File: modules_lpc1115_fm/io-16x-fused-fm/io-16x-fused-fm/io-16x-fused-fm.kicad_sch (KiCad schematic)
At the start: 143 parts, among them IC5 LPC1115, IC6 ATAES132A-SHEQ-T, J1 62000611622, J2 1771017, J3 1770953, Q3 ASF, U3 EEPROM, X1 MICROMATCH-10SMD

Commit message: convert io-16x-fused-fm WIP
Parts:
- C1, C2, C25, C26, C27, C28, C29, C30, C31, C32, C33, C34, C35, C36: footprint io-16x-fused-fm:C0805 -> Capacitor_SMD:C_0805_2012Metric; symbol io-16x-fused-fm-eagle-import:C-EUC0805 -> Device:C
- D1, D13, D14, D15, D16, D17, D18, D19, D2, D20, D3, D4, D5, D6, D7, D8: footprint io-16x-fused-fm:SOD-123 -> Diode_SMD:D_SOD-123; symbol io-16x-fused-fm-eagle-import:DIODE-ZENERSOD-123 -> Device:D_Zener
- D10, D11, D12, D21, D22, D23, D24, D9: footprint io-16x-fused-fm:SOT23 -> Package_TO_SOT_SMD:SOT-23; symbol io-16x-fused-fm-eagle-import:BAT54C -> Diode:BAT54C
- F1, F10, F11, F12, F13, F14, F15, F16, F2, F3, F4, F5, F6, F7, F8, F9: footprint io-16x-fused-fm:0805L -> Fuse:Fuse_0805_2012Metric; symbol io-16x-fused-fm-eagle-import:?0805L -> Device:Polyfuse
- FB1, FB17, FB18, FB19, FB2, FB20, FB21, FB22, FB23, FB24, FB3, FB4, FB5, FB6, FB7, FB8: footprint io-16x-fused-fm:FERR_0805MP -> Inductor_SMD:L_0805_2012Metric; symbol io-16x-fused-fm-eagle-import:FERRITE2_0805MP -> Device:FerriteBead
- IC6: footprint io-16x-fused-fm:SOIC127P600X175-8N -> Package_SO:SOIC-8_3.9x4.9mm_P1.27mm; symbol io-16x-fused-fm-eagle-import:ATAES132A-SHEQ-T -> Memory_EEPROM:25LCxxx
- J2: symbol io-16x-fused-fm-eagle-import:1771017 -> Connector_Generic:Conn_01x08
- J3: symbol io-16x-fused-fm-eagle-import:1770953 -> Connector_Generic:Conn_01x02
- JP1: value PINHD-1X06_2.54-S -> Conn_01x06_Pin; symbol io-16x-fused-fm-eagle-import:PINHD-1X06_2.54-S -> Connector:Conn_01x06_Pin
- JP17: value J -> Conn_02x05_Odd_Even; symbol io-16x-fused-fm-eagle-import:PINHD-2X05_2.00 -> Connector_Generic:Conn_02x05_Odd_Even
- JP18, JP21, JP24: symbol io-16x-fused-fm-eagle-import:PINHD-1X2 -> Connector:Conn_01x02_Pin
- JP2: symbol io-16x-fused-fm-eagle-import:PINHD-1X5 -> Connector:Conn_01x05_Pin
- JP22: symbol io-16x-fused-fm-eagle-import:62000411622 -> Connector:Conn_01x04_Pin
- JP23: value PINHD-1X4 -> Conn_01x04_Pin; symbol io-16x-fused-fm-eagle-import:PINHD-1X4 -> Connector:Conn_01x04_Pin
- LED5, LED6: footprint io-16x-fused-fm:CHIPLED_0805 -> LED_SMD:LED_0805_2012Metric; symbol io-16x-fused-fm-eagle-import:LEDCHIPLED_0805 -> Device:LED
- PRGBTN2: footprint io-16x-fused-fm:1X01 -> Connector_PinSocket_2.54mm:PinSocket_1x01_P2.54mm_Horizontal; symbol io-16x-fused-fm-eagle-import:PINHD-1X1 -> Connector:Conn_01x01_Pin
- R1, R10, R11, R12, R13, R14, R15, R16, R2, R3, R4, R5, R55, R56, R57, R58, R59, R6, R60, R61, R62, R63, R64, R65, R66, R67, R68, R69, R7, R70, R71, R72, R73, R74, R75, R76, R77, R78, R79, R8, R80, R81, R9: footprint io-16x-fused-fm:R0805 -> Resistor_SMD:R_0805_2012Metric; symbol io-16x-fused-fm-eagle-import:R-EU_R0805 -> Device:R
- TP1, TP2, TP3, TP4, TP5, TP6: footprint io-16x-fused-fm:TP08R -> TestPoint:TestPoint_Pad_D1.0mm; symbol io-16x-fused-fm-eagle-import:TPSQTP08R -> Connector:TestPoint
- TVS1, TVS2, TVS5, TVS6, TVS9: footprint io-16x-fused-fm:SOT-23-6L -> Package_TO_SOT_SMD:SOT-23-6; symbol io-16x-fused-fm-eagle-import:USBLC6-4SC6 -> Power_Protection:USBLC6-4SC6
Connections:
- net +3V3: now also J3.2 (Pin_2), JP22.2 (Pin_2), LED6.2 (A); no longer IC6.3 (NC_1), IC6.7 (NC_2), J3.3 (2.1), J3.4 (2.2), JP22.3
- net GND: now also D1.2 (A), D13.2 (A), D14.2 (A), D15.2 (A), D16.2 (A), D17.2 (A), D18.2 (A), D19.2 (A), D2.2 (A), D20.2 (A), D3.2 (A), D4.2 (A), D5.2 (A), D6.2 (A), D7.2 (A), D8.2 (A), JP22.1 (Pin_1); no longer D1.A, D13.A, D14.A, D15.A, D16.A, D17.A, D18.A, D19.A, D2.A, D20.A, D3.A, D4.A, D5.A, D6.A, D7.A, D8.A, J3.2 (1.2), JP22.4
- net IN1: no longer J2.2 (1.2)
- net IN2: now also J2.2 (Pin_2); no longer J2.3 (2.1), J2.4 (2.2)
- net IN3: now also J2.3 (Pin_3); no longer J2.5 (3.1), J2.6 (3.2)
- net IN4: now also J2.4 (Pin_4); no longer J2.7 (4.1), J2.8 (4.2)
- net IN5: now also J2.5 (Pin_5); no longer J2.10 (5.2), J2.9 (5.1)
- net IN6: now also J2.6 (Pin_6); no longer J2.11 (6.1), J2.12 (6.2)
- net IN7: now also J2.7 (Pin_7); no longer J2.13 (7.1), J2.14 (7.2)
- net IN8: now also J2.8 (Pin_8); no longer J2.15 (8.1), J2.16 (8.2)
- net IO1R: now also D19.1 (K); no longer D19.C
- net IO2R: now also D20.1 (K); no longer D20.C
- net IO3R: now also D17.1 (K); no longer D17.C
- net IO4R: now also D18.1 (K); no longer D18.C
- net IO5R: now also D13.1 (K); no longer D13.C
- net IO6R: now also D14.1 (K); no longer D14.C
- net IO7R: now also D16.1 (K); no longer D16.C
- net IO8R: now also D15.1 (K); no longer D15.C
- net N$10: now also F5.1; no longer F5.2
- net N$11: now also F10.1; no longer F10.2
- net N$12: now also F6.1; no longer F6.2
- net N$13: now also F15.1; no longer F15.2
- net N$14: now also F7.1; no longer F7.2
- net N$15: now also F11.1; no longer F11.2
- net N$16: now also F16.1; no longer F16.2
- net N$17: now also F8.1; no longer F8.2
- net N$2: now also F13.1; no longer F13.2
- net N$3: now also F14.1; no longer F14.2
- net N$4: now also F12.1; no longer F12.2
- net N$5: now also F9.1; no longer F9.2
- net PROG: now also LED5.1 (K); no longer LED5.C
- net SCL: now also JP22.4 (Pin_4); no longer JP22.1
- net SDA: now also JP22.3 (Pin_3); no longer JP22.2
- net at FB7.2: now also F7.2; no longer F7.1
- net at FB5.2: now also F5.2; no longer F5.1
- net at IC5.32 (TDI/PIO0_11/AD0/CT32B0_MAT3): now also TP2.1; no longer TP2.TP
- net at D10.2, R1.2, R12.1: now also D1.1 (K); no longer D1.C
- net at FB18.1: now also F10.2; no longer F10.1
- net at D10.1, R2.2, R9.1: now also D2.1 (K); no longer D2.C
- net at D11.2, R14.1, R7.2: now also D6.1 (K); no longer D6.C
- net at D9.1, R10.1, R3.2: now also D3.1 (K); no longer D3.C
- net at D9.2, R11.1, R4.2: now also D4.1 (K); no longer D4.C
- net at IC5.45 (PIO1_5/RTS/CT32B0_CAP0): now also TP6.1; no longer TP6.TP
- net at R1.1: now also F1.1, TVS1.4 (I/O3); no longer F1.2
- net at R57.1: now also LED5.2 (A); no longer LED5.A
- net at FB17.1: now also F9.2; no longer F9.1
- net at IC5.34 (TDO/PIO1_1/AD2/CT32B1_MAT0): now also TP4.1; no longer TP4.TP
- net at FB8.2: now also F8.2; no longer F8.1
- net at D11.1, R15.1, R8.2: now also D5.1 (K); no longer D5.C
- net at D12.2, R13.1, R6.2: now also D7.1 (K); no longer D7.C
- net at D12.1, R16.1, R5.2: now also D8.1 (K); no longer D8.C
- net at FB20.1: now also F12.2; no longer F12.1
- net at IC5.33 (TMS/PIO1_0/AD1/CT32B1_CAP0): now also TP3.1; no longer TP3.TP
- net at IC5.31 (PIO2_11/SCK0/CT32B0_CAP1): now also TP1.1; no longer TP1.TP
- net at FB19.1: now also F11.2; no longer F11.1
- net at R3.1, TVS1.6 (I/O4): now also F3.1; no longer F3.2
- net at FB6.2: now also F6.2; no longer F6.1
- net at F4.1: now also R4.1, TVS1.1 (I/O1); no longer FB4.1 (P$1)
- net at FB23.1: now also F14.2; no longer F14.1
- net at FB21.1: now also F16.2; no longer F16.1
- net at R2.1, TVS1.3 (I/O2): now also F2.1; no longer F2.2
- net at FB3.1: now also F3.2; no longer F3.1
- net at FB1.1: now also F1.2; no longer F1.1
- net at R81.2: now also LED6.1 (K); no longer LED6.C
- net at IC5.35 (TRST/PIO1_2/AD3/CT32B1_MAT1): now also TP5.1; no longer TP5.TP
- net at FB2.1: now also F2.2; no longer F2.1
- net at FB24.1: now also F13.2; no longer F13.1
- net at FB22.1: now also F15.2; no longer F15.1
- new net: F4.2, FB4.1
- no-connect marks 0 -> 7
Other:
- moved on the sheet: JP18, JP21, JP22, JP24

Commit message: bump io-16x-fused-fm - conversion mostly done
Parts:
- IC5: value LPC1115 -> LPC1115FBD48-303; footprint io-16x-fused-fm:LQFP48 -> Package_QFP:LQFP-48_7x7mm_P0.5mm; symbol io-16x-fused-fm-eagle-import:LPC1113/4/5_QFP48_XLSERIES -> MCU_NXP_LPC:LPC1115FBD48-303
- J1: value 62000611622 -> Conn_01x06; footprint io-16x-fused-fm:62000611622 -> Connector_JST:JST_PH_B6B-PH-K_1x06_P2.00mm_Vertical; symbol io-16x-fused-fm-eagle-import:62000611622 -> Connector_Generic:Conn_01x06
- J2: footprint io-16x-fused-fm:1771017 -> TerminalBlock_Phoenix:TerminalBlock_Phoenix_PTSM-0,5-8-2.5-V-THR_1x08_P2.50mm_Vertical
- J3: footprint io-16x-fused-fm:1770953 -> TerminalBlock_Phoenix:TerminalBlock_Phoenix_PTSM-0,5-2-2.5-V-THR_1x02_P2.50mm_Vertical
- JP1: footprint io-16x-fused-fm:1X06-S -> Connector_PinHeader_2.54mm:PinHeader_1x06_P2.54mm_Vertical
- JP17: footprint io-16x-fused-fm:2X05M -> Connector_PinHeader_2.00mm:PinHeader_2x05_P2.00mm_Vertical
- JP18, JP21, JP24: footprint io-16x-fused-fm:1X02 -> Connector_PinHeader_2.54mm:PinHeader_1x02_P2.54mm_Vertical
- JP2: footprint io-16x-fused-fm:1X05 -> Connector_PinHeader_2.54mm:PinHeader_1x05_P2.54mm_Vertical
- JP22: value 62000411622 -> Conn_01x04; footprint io-16x-fused-fm:62000411622 -> Connector_JST:JST_PH_B4B-PH-K_1x04_P2.00mm_Vertical; symbol Connector:Conn_01x04_Pin -> Connector_Generic:Conn_01x04
- JP23: footprint io-16x-fused-fm:1X04 -> Connector_PinHeader_2.54mm:PinHeader_1x04_P2.54mm_Vertical
- PRGBTN2: footprint Connector_PinSocket_2.54mm:PinSocket_1x01_P2.54mm_Horizontal -> Connector_PinHeader_2.54mm:PinHeader_1x01_P2.54mm_Vertical; now not fitted; now left out of the parts list
- Q3: value ASF -> 12 MHz; footprint io-16x-fused-fm:ASF -> Oscillator:Oscillator_SMD_SeikoEpson_SG210-4Pin_2.5x2.0mm; symbol io-16x-fused-fm-eagle-import:ASF -> Oscillator:SG-210STF
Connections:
- net +3V3: now also IC6.3 (~{WP}), IC6.7 (~{HOLD}), JP22.3 (Pin_3); no longer JP22.2 (Pin_2)
- net GND: now also JP18.1 (Pin_1), JP22.4 (Pin_4); no longer JP18.2 (Pin_2), JP22.1 (Pin_1)
- net N$10: now also F5.2; no longer F5.1
- net N$11: now also F10.2; no longer F10.1
- net N$12: now also F6.2; no longer F6.1
- net N$13: now also F15.2; no longer F15.1
- net N$14: now also F7.2; no longer F7.1
- net N$15: now also F11.2; no longer F11.1
- net N$16: now also F16.2; no longer F16.1
- net N$17: now also F8.2; no longer F8.1
- net N$2: now also F13.2; no longer F13.1
- net N$3: now also F14.2; no longer F14.1
- net N$4: now also F12.2; no longer F12.1
- net N$5: now also F9.2; no longer F9.1
- net PROG: now also JP18.2 (Pin_2); no longer JP18.1 (Pin_1)
- net SCL: now also JP22.1 (Pin_1); no longer JP22.4 (Pin_4)
- net SDA: now also JP22.2 (Pin_2); no longer JP22.3 (Pin_3)
- net at FB7.2: now also F7.1; no longer F7.2
- net at FB5.2: now also F5.1; no longer F5.2
- net at FB18.1: now also F10.1; no longer F10.2
- net at R1.1, TVS1.4 (I/O3): now also F1.2; no longer F1.1
- net at FB17.1: now also F9.1; no longer F9.2
- net at FB8.2: now also F8.1; no longer F8.2
- net at FB20.1: now also F12.1; no longer F12.2
- net at FB19.1: now also F11.1; no longer F11.2
- net at R3.1, TVS1.6 (I/O4): now also F3.2; no longer F3.1
- net at FB6.2: now also F6.1; no longer F6.2
- net at R4.1, TVS1.1 (I/O1): now also F4.2; no longer F4.1
- net at FB4.1: now also F4.1; no longer F4.2
- net at FB23.1: now also F14.1; no longer F14.2
- net at FB21.1: now also F16.1; no longer F16.2
- net at R2.1, TVS1.3 (I/O2): now also F2.2; no longer F2.1
- net at FB3.1: now also F3.1; no longer F3.2
- net at FB1.1: now also F1.1; no longer F1.2
- net at FB2.1: now also F2.1; no longer F2.2
- net at FB24.1: now also F13.1; no longer F13.2
- net at FB22.1: now also F15.1; no longer F15.2
- no-connect marks 7 -> 5
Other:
- moved on the sheet: C25, C27, C28, C29, C30, C31, C34, F1, F10, F11, F12, F13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

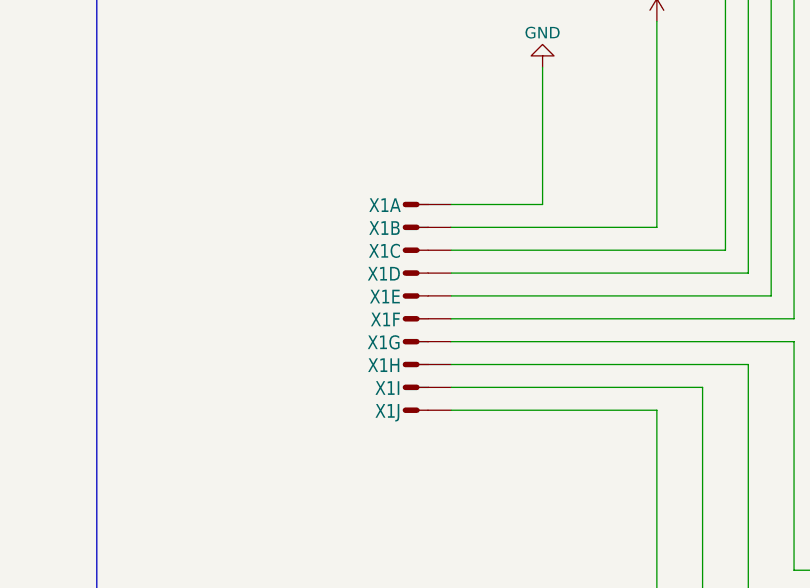
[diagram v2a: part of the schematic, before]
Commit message: io-16x-fused-fm: use micro-match from selfbus library
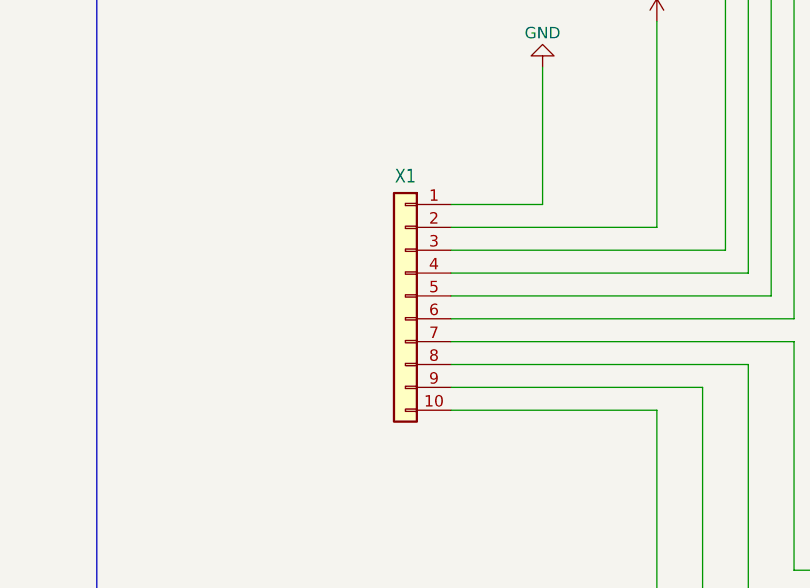
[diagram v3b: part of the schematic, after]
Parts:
- removed unit 10 of X1
- removed unit 3 of X1
- removed unit 5 of X1
- removed unit 7 of X1
- removed unit 4 of X1
- removed unit 8 of X1
- removed unit 6 of X1
- removed unit 2 of X1
- removed unit 9 of X1
- JP1: footprint Connector_PinHeader_2.54mm:PinHeader_1x06_P2.54mm_Vertical -> selfbus:PinHeader_1x06_P2.54mm_Vertical_no_silkscreen
- JP23: footprint Connector_PinHeader_2.54mm:PinHeader_1x04_P2.54mm_Vertical -> selfbus:PinHeader_1x04_P2.54mm_Vertical_no_silkscreen
- U3: footprint io-16x-fused-fm:SOT23-5 -> Package_TO_SOT_SMD:SOT-23-5
- X1: footprint io-16x-fused-fm:MICROMATCH-10SMD -> selfbus:TE_Connectivity_MICRO-MATCH_SMD_FTE_1-188275-0_2x05_P1.27mm_Vertical; symbol io-16x-fused-fm-eagle-import:MICROMATCH-10SMD -> Connector_Generic:Conn_01x10
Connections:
- net +3V3: now also X1.2 (Pin_2)
- net N$22: now also X1.4 (Pin_4)
- net at FB5.1: now also X1.7 (Pin_7)
- net at FB7.1: now also X1.9 (Pin_9)
- net at FB8.1: now also X1.10 (Pin_10)
- net at FB1.2: now also X1.3 (Pin_3)
- net at FB3.2: now also X1.5 (Pin_5)
- net at FB6.1: now also X1.8 (Pin_8)
- net at FB4.2: now also X1.6 (Pin_6)

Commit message: finally standardize selected parts on all boards
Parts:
- C1, C2: value 100nF -> 100n; now left out of the parts list
- C25, C28: value 1uF -> 1u
- C26, C31: value 10nF -> 10n
- C27, C32, C33, C34, C35, C36: value 100nF -> 100n
- C29: value 220pF -> 220p
- C30: value 100pF -> 100p
- D1, D10, D11, D12, D2, D3, D4, D5, D6, D7, D8, D9, FB1, FB2, FB3, FB4, FB5, FB6, FB7, FB8, R1, R10, R11, R12, R13, R14, R15, R16, R2, R3, R4, R5, R6, R7, R8, R9, TVS1, TVS2: now left out of the parts list
- F1, F2, F3, F4, F5, F6, F7, F8: value ?0805L -> BSMD0805-005-33V; now left out of the parts list
- F10, F11, F12, F13, F14, F15, F16, F9: value ?0805L -> BSMD0805-005-33V
- JP1, JP23: now not fitted; now left out of the parts list
- Q3: value 12 MHz -> 12MHz
- R70, R71: value 3,3k -> 3k3
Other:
- note added: "BOTTOM IOs - standardmäßig NICHT auf BOM enthalten"
- note removed: "BOTTOM IOs"

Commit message: final for manufacturing
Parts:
- R10, R11, R12, R13, R14, R15, R16, R73, R74, R75, R76, R77, R78, R79, R80, R9: value 100R -> 100
- U3: value EEPROM -> MCP24AA32 EEPROM; symbol io-16x-fused-fm-eagle-import:EEPROM_I2C_MCP24AA32 -> Memory_EEPROM:24AA02-OT
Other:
- moved on the sheet: C35

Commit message: update io-16x-fused-fm
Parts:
- TP1, TP2, TP3, TP4, TP5, TP6: now left out of the parts list
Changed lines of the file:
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@@
 		(unit 1)
 		(exclude_from_sim no)
-		(in_bom yes)
+		(in_bom no)
 		(on_board yes)
 		(dnp no)
@@
 		(unit 1)
 		(exclude_from_sim no)
-		(in_bom yes)
+		(in_bom no)
 		(on_board yes)
 		(dnp no)
@@
 		(unit 1)
 		(exclude_from_sim no)
-		(in_bom yes)
+		(in_bom no)
 		(on_board yes)
 		(dnp no)
@@
 		(unit 1)
 		(exclude_from_sim no)
-		(in_bom yes)
+		(in_bom no)
 		(on_board yes)
 		(dnp no)
@@
 		(unit 1)
 		(exclude_from_sim no)
-		(in_bom yes)
+		(in_bom no)
 		(on_board yes)
 		(dnp no)
@@
 		(unit 1)
 		(exclude_from_sim no)
-		(in_bom yes)
+		(in_bom no)
 		(on_board yes)
 		(dnp no)

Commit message: update xtal caps, eib_in cap+resistor, bus_v resistors
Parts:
- C29: value 220p -> 22p
- C30: value 100p -> 22p
- C35, C36, IC6, JP18, JP24, U3: now not fitted; now left out of the parts list
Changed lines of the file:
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@@
 	)
 	(junction
-		(at 533.4 459.74)
-		(diameter 0)
-		(color 0 0 0 0)
-	)
-	(junction
 		(at 581.66 129.54)
 		(diameter 0)
@@
 	)
 	(junction
+		(at 529.59 461.01)
+		(diameter 0)
+		(color 0 0 0 0)
+	)
+	(junction
 		(at 673.1 193.04)
 		(diameter 0)
@@
 	(wire
 		(pts
+			(xy 529.59 461.01) (xy 529.59 463.55)
+		)
+		(stroke
+			(width 0.1524)
+			(type solid)
+		)
+	)
+	(wire
+		(pts
 			(xy 304.8 208.28) (xy 304.8 246.38)
 		)
@@
 	(wire
 		(pts
-			(xy 523.24 459.74) (xy 513.08 459.74)
-		)
-		(stroke
-			(width 0.1524)
-			(type solid)
-		)
-	)
-	(wire
-		(pts
 			(xy 217.17 469.9) (xy 213.36 469.9)
 		)
@@
 	(wire
 		(pts
+			(xy 558.8 461.01) (xy 558.8 459.74)
+		)
+		(stroke
+			(width 0)
+			(type default)
+		)
+	)
+	(wire
+		(pts
 			(xy 223.52 256.54) (xy 223.52 250.19)
 		)
@@
 	(wire
 		(pts
-			(xy 513.08 434.34) (xy 541.02 434.34)
+			(xy 529.59 434.34) (xy 541.02 434.34)
 		)
 		(stroke
@@
 	(wire
 		(pts
-			(xy 533.4 459.74) (xy 533.4 462.28)
-		)
-		(stroke
-			(width 0.1524)
-			(type solid)
-		)
-	)
-	(wire
-		(pts
 			(xy 654.05 198.12) (xy 654.05 193.04)
 		)
@@
 	(wire
 		(pts
-			(xy 533.4 459.74) (xy 543.56 459.74)
-		)
-		(stroke
-			(width 0.1524)
-			(type solid)
-		)
-	)
-	(wire
-		(pts
 			(xy 110.49 160.02) (xy 109.22 160.02)
 		)
@@
 	(wire
 		(pts
-			(xy 513.08 434.34) (xy 513.08 459.74)
+			(xy 529.59 434.34) (xy 529.59 443.23)
 		)
 		(stroke
@@
 	(wire
 		(pts
-			(xy 530.86 459.74) (xy 533.4 459.74)
-		)
-		(stroke
-			(width 0.1524)
-			(type solid)
-		)
-	)
-	(wire
-		(pts
 			(xy 586.74 231.14) (xy 623.57 231.14)
 		)
@@
 	(wire
 		(pts
-			(xy 558.8 459.74) (xy 543.56 459.74)
+			(xy 544.83 461.01) (xy 558.8 461.01)
 		)
 		(stroke
@@
 	(wire
 		(pts
+			(xy 529.59 450.85) (xy 529.59 461.01)
+		)
+		(stroke
+			(width 0.1524)
+			(type solid)
+		)
+	)
+	(wire
+		(pts
 			(xy 212.09 487.68) (xy 212.09 490.22)
 		)
@@
 	(wire
 		(pts
+			(xy 529.59 461.01) (xy 544.83 461.01)
+		)
+		(stroke
+			(width 0.1524)
+			(type solid)
+		)
+	)
+	(wire
+		(pts
 			(xy 129.54 457.2) (xy 149.86 457.2)
 		)
@@
 		(fields_autoplaced yes)
 		(property "Reference" "C30"
-			(at 217.17 478.79 90)
+			(at 217.17 480.3264 90)
 			(effects
 				(font
@@
 			)
 		)
-		(property "Value" "100p"
-			(at 217.17 482.6 90)
+		(property "Value" "22p"
+			(at 217.17 483.4508 90)
 			(effects
 				(font
@@
 		(unit 1)
 		(exclude_from_sim no)
-		(in_bom yes)
+		(in_bom no)
 		(on_board yes)
-		(dnp no)
+		(dnp yes)
 		(fields_autoplaced yes)
 		(property "Reference" "JP24"
@@
 	(symbol
 		(lib_id "Device:C")
-		(at 527.05 459.74 90)
-		(mirror x)
+		(at 529.59 447.04 0)
+		(mirror y)
 		(unit 1)
 		(exclude_from_sim no)
-		(in_bom yes)
+		(in_bom no)
 		(on_board yes)
-		(dnp no)
+		(dnp yes)
 		(fields_autoplaced yes)
 		(property "Reference" "C36"
-			(at 527.05 452.3864 90)
+			(at 532.511 445.4778 0)
 			(effects
 				(font
 					(size 1.778 1.5113)
 				)
+				(justify right)
 			)
 		)
 		(property "Value" "100n"
-			(at 527.05 455.5108 90)
+			(at 532.511 448.6022 0)
 			(effects
 				(font
 					(size 1.778 1.5113)
 				)
+				(justify right)
 			)
 		)
 		(property "Footprint" "Capacitor_SMD:C_0805_2012Metric"
-			(at 530.86 460.7052 0)
+			(at 528.6248 450.85 0)
 			(effects
 				(font
@@
 		)
 		(property "Datasheet" "~"
-			(at 527.05 459.74 0)
+			(at 529.59 447.04 0)
 			(effects
 				(font
@@
 		)
 		(property "Description" "Unpolarized capacitor"
-			(at 527.05 459.74 0)
+			(at 529.59 447.04 0)
 			(effects
 				(font
@@
 		(unit 1)
 		(exclude_from_sim no)
-		(in_bom yes)
+		(in_bom no)
 		(on_board yes)
-		(dnp no)
+		(dnp yes)
 		(property "Reference" "U3"
 			(at 408.94 452.3195 0)
@@
 	(symbol
 		(lib_id "power:GND")
-		(at 533.4 462.28 0)
+		(at 529.59 463.55 0)
 		(unit 1)
 		(exclude_from_sim no)
@@
 		(fields_autoplaced yes)
 		(property "Reference" "#PWR069"
-			(at 533.4 468.63 0)
+			(at 529.59 469.9 0)
 			(effects
 				(font
@@
 		)
 		(property "Value" "GND"
-			(at 533.4 466.4131 0)
+			(at 529.59 467.6831 0)
 			(effects
 				(font
@@
 		)
 		(property "Footprint" ""
-			(at 533.4 462.28 0)
+			(at 529.59 463.55 0)
 			(effects
 				(font
@@
 		)
 		(property "Datasheet" ""
-			(at 533.4 462.28 0)
+			(at 529.59 463.55 0)
 			(effects
 				(font
@@
 		)
 		(property "Description" "Power symbol creates a global label with name \"GND\" , ground"
-			(at 533.4 462.28 0)
+			(at 529.59 463.55 0)
 			(effects
 				(font
@@
 		(unit 1)
 		(exclude_from_sim no)
-		(in_bom yes)
+		(in_bom no)
 		(on_board yes)
-		(dnp no)
+		(dnp yes)
 		(property "Reference" "JP18"
 			(at 724.6112 372.11 0)
@@
 		(unit 1)
 		(exclude_from_sim no)
-		(in_bom yes)
+		(in_bom no)
 		(on_board yes)
-		(dnp no)
+		(dnp yes)
 		(fields_autoplaced yes)
 		(property "Reference" "C35"
@@
 		(unit 1)
 		(exclude_from_sim no)
-		(in_bom yes)
+		(in_bom no)
 		(on_board yes)
-		(dnp no)
+		(dnp yes)
 		(fields_autoplaced yes)
 		(property "Reference" "IC6"
@@
 			)
 		)
-		(property "Value" "220p"
+		(property "Value" "22p"
 			(at 209.169 495.5922 0)
 			(effects
